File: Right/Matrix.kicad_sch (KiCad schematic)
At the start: 80 parts, among them SW201 SW_Push, SW202 SW_Push, SW203 SW_Push, SW204 SW_Push, SW205 SW_Push, SW206 SW_Push, SW207 SW_Push, SW208 SW_Push, SW209 SW_Push, SW210 SW_Push, SW211 SW_Push, SW212 SW_Push, SW213 SW_Push, SW214 SW_Push, SW215 SW_Push, SW216 SW_Push, SW217 SW_Push, SW218 SW_Push, SW219 SW_Push

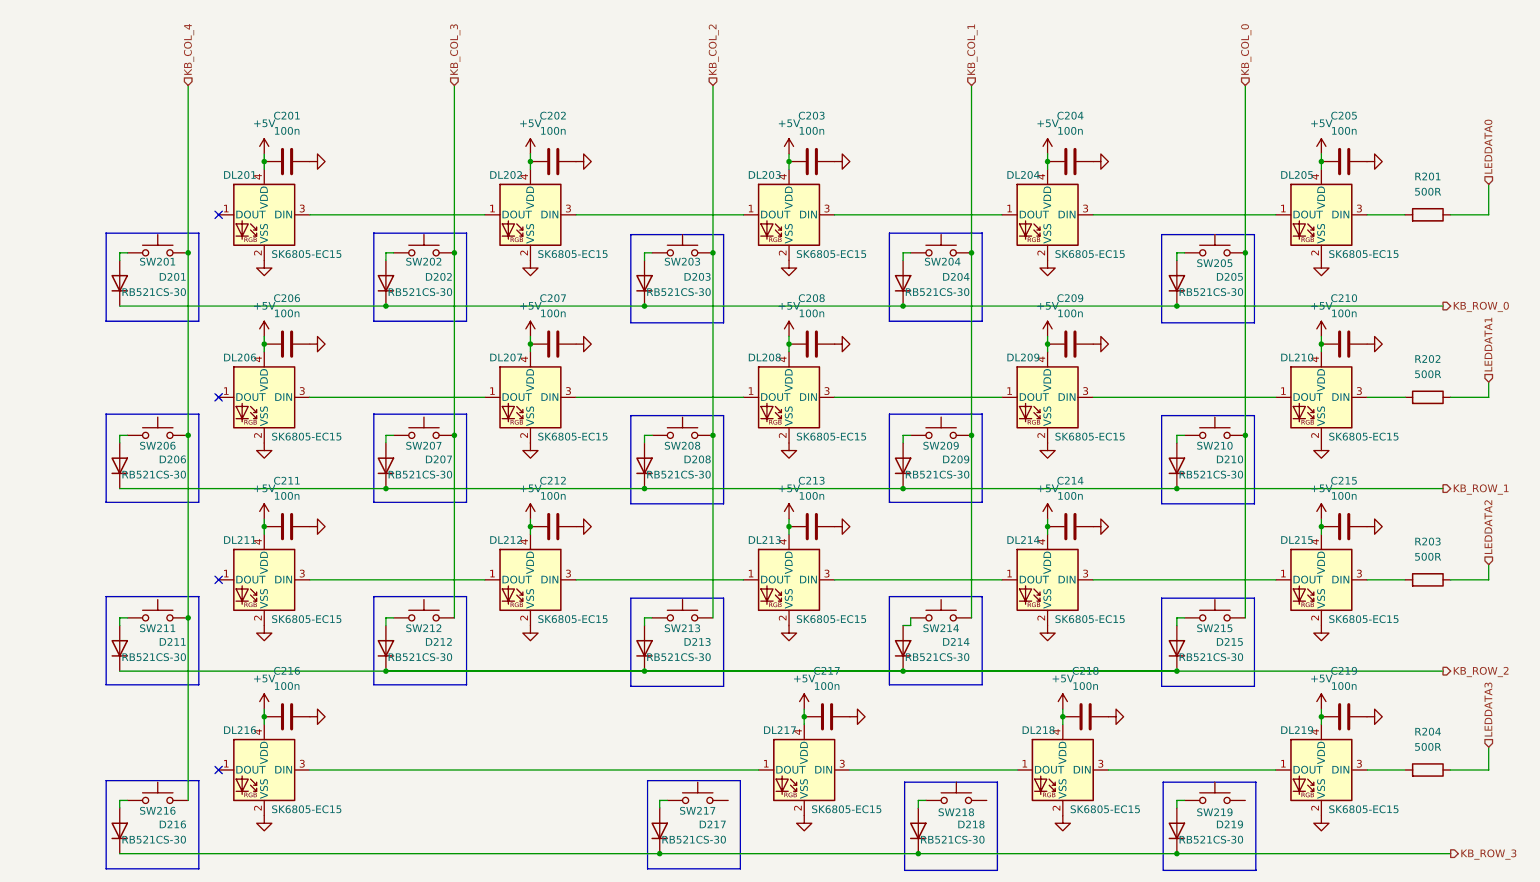
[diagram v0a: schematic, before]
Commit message: redesign with smaller components
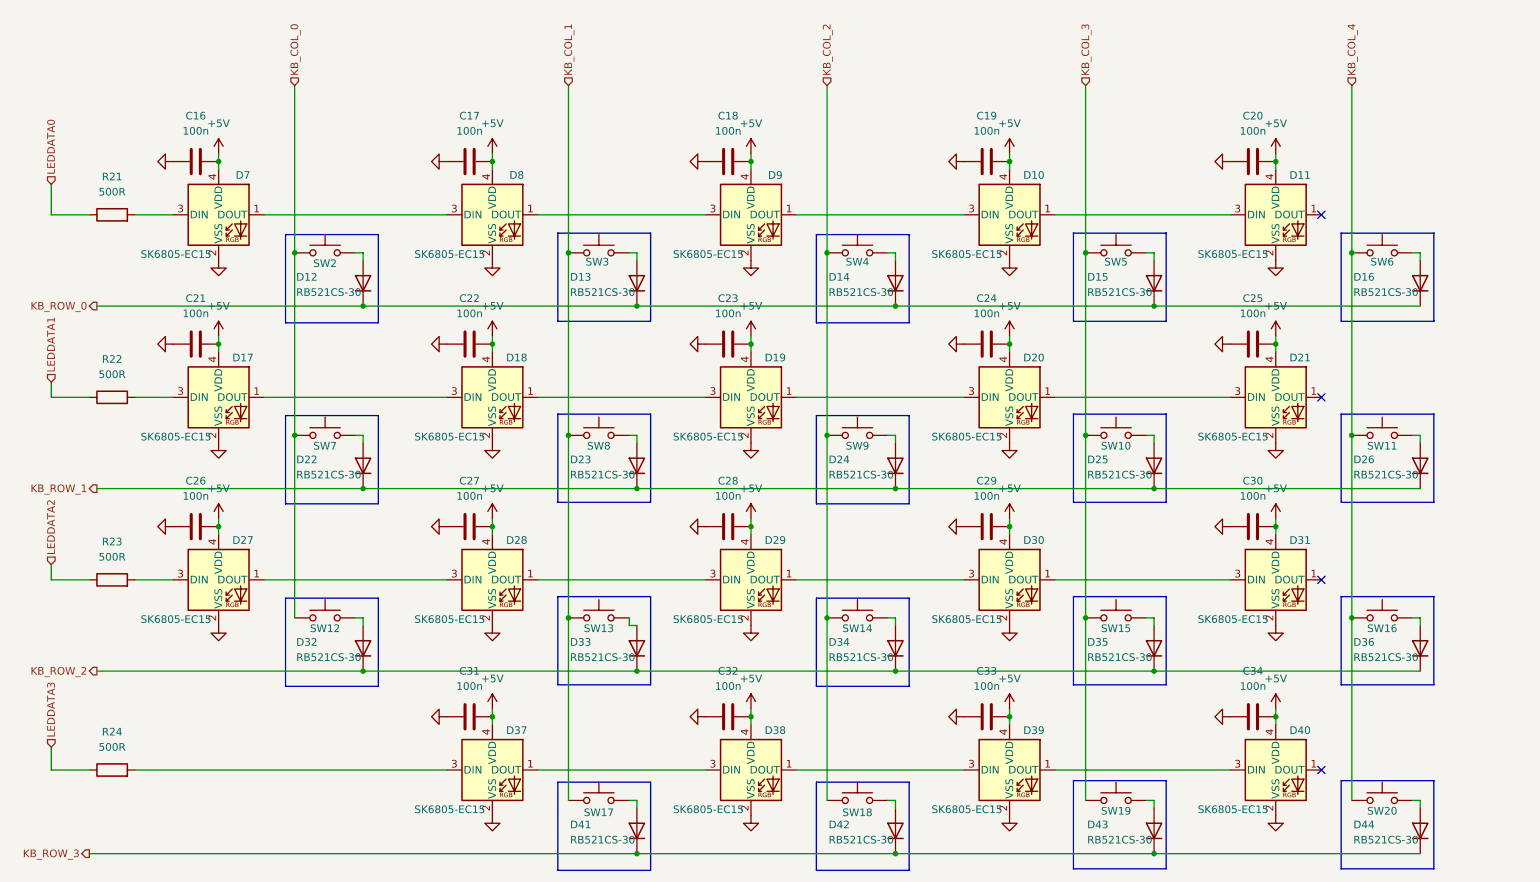
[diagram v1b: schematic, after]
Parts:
- C16: renamed from C205; footprint Capacitor_SMD:C_0603_1608Metric_Pad1.08x0.95mm_HandSolder -> Capacitor_SMD:C_0402_1005Metric_Pad0.74x0.62mm_HandSolder
- C17: renamed from C204; footprint Capacitor_SMD:C_0603_1608Metric_Pad1.08x0.95mm_HandSolder -> Capacitor_SMD:C_0402_1005Metric_Pad0.74x0.62mm_HandSolder
- C18: renamed from C203; footprint Capacitor_SMD:C_0603_1608Metric_Pad1.08x0.95mm_HandSolder -> Capacitor_SMD:C_0402_1005Metric_Pad0.74x0.62mm_HandSolder
- C19: renamed from C202; footprint Capacitor_SMD:C_0603_1608Metric_Pad1.08x0.95mm_HandSolder -> Capacitor_SMD:C_0402_1005Metric_Pad0.74x0.62mm_HandSolder
- C20: renamed from C201; footprint Capacitor_SMD:C_0603_1608Metric_Pad1.08x0.95mm_HandSolder -> Capacitor_SMD:C_0402_1005Metric_Pad0.74x0.62mm_HandSolder
- C21: renamed from C210; footprint Capacitor_SMD:C_0603_1608Metric_Pad1.08x0.95mm_HandSolder -> Capacitor_SMD:C_0402_1005Metric_Pad0.74x0.62mm_HandSolder
- C22: renamed from C209; footprint Capacitor_SMD:C_0603_1608Metric_Pad1.08x0.95mm_HandSolder -> Capacitor_SMD:C_0402_1005Metric_Pad0.74x0.62mm_HandSolder
- C23: renamed from C208; footprint Capacitor_SMD:C_0603_1608Metric_Pad1.08x0.95mm_HandSolder -> Capacitor_SMD:C_0402_1005Metric_Pad0.74x0.62mm_HandSolder
- C24: renamed from C207; footprint Capacitor_SMD:C_0603_1608Metric_Pad1.08x0.95mm_HandSolder -> Capacitor_SMD:C_0402_1005Metric_Pad0.74x0.62mm_HandSolder
- C25: renamed from C206; footprint Capacitor_SMD:C_0603_1608Metric_Pad1.08x0.95mm_HandSolder -> Capacitor_SMD:C_0402_1005Metric_Pad0.74x0.62mm_HandSolder
- C26: renamed from C215; footprint Capacitor_SMD:C_0603_1608Metric_Pad1.08x0.95mm_HandSolder -> Capacitor_SMD:C_0402_1005Metric_Pad0.74x0.62mm_HandSolder
- C27: renamed from C214; footprint Capacitor_SMD:C_0603_1608Metric_Pad1.08x0.95mm_HandSolder -> Capacitor_SMD:C_0402_1005Metric_Pad0.74x0.62mm_HandSolder
- C28: renamed from C213; footprint Capacitor_SMD:C_0603_1608Metric_Pad1.08x0.95mm_HandSolder -> Capacitor_SMD:C_0402_1005Metric_Pad0.74x0.62mm_HandSolder
- C29: renamed from C212; footprint Capacitor_SMD:C_0603_1608Metric_Pad1.08x0.95mm_HandSolder -> Capacitor_SMD:C_0402_1005Metric_Pad0.74x0.62mm_HandSolder
- C30: renamed from C211; footprint Capacitor_SMD:C_0603_1608Metric_Pad1.08x0.95mm_HandSolder -> Capacitor_SMD:C_0402_1005Metric_Pad0.74x0.62mm_HandSolder
- C31: renamed from C219; footprint Capacitor_SMD:C_0603_1608Metric_Pad1.08x0.95mm_HandSolder -> Capacitor_SMD:C_0402_1005Metric_Pad0.74x0.62mm_HandSolder
- C32: renamed from C218; footprint Capacitor_SMD:C_0603_1608Metric_Pad1.08x0.95mm_HandSolder -> Capacitor_SMD:C_0402_1005Metric_Pad0.74x0.62mm_HandSolder
- C33: renamed from C217; footprint Capacitor_SMD:C_0603_1608Metric_Pad1.08x0.95mm_HandSolder -> Capacitor_SMD:C_0402_1005Metric_Pad0.74x0.62mm_HandSolder
- C34: renamed from C216; footprint Capacitor_SMD:C_0603_1608Metric_Pad1.08x0.95mm_HandSolder -> Capacitor_SMD:C_0402_1005Metric_Pad0.74x0.62mm_HandSolder
- R21: renamed from R201; footprint Resistor_SMD:R_0603_1608Metric_Pad0.98x0.95mm_HandSolder -> Resistor_SMD:R_0402_1005Metric_Pad0.72x0.64mm_HandSolder
- R22: renamed from R202; footprint Resistor_SMD:R_0603_1608Metric_Pad0.98x0.95mm_HandSolder -> Resistor_SMD:R_0402_1005Metric_Pad0.72x0.64mm_HandSolder
- R23: renamed from R203; footprint Resistor_SMD:R_0603_1608Metric_Pad0.98x0.95mm_HandSolder -> Resistor_SMD:R_0402_1005Metric_Pad0.72x0.64mm_HandSolder
- R24: renamed from R204; footprint Resistor_SMD:R_0603_1608Metric_Pad0.98x0.95mm_HandSolder -> Resistor_SMD:R_0402_1005Metric_Pad0.72x0.64mm_HandSolder
- renumbered DL202 to D10, DL201 to D11, D205 to D12, D204 to D13, D203 to D14, D202 to D15, D201 to D16, DL210 to D17, DL209 to D18, DL208 to D19, DL207 to D20, DL206 to D21, D210 to D22, D209 to D23, D208 to D24, D207 to D25, D206 to D26, DL215 to D27, DL214 to D28, DL213 to D29, DL212 to D30, DL211 to D31, D215 to D32, D214 to D33, D213 to D34, D212 to D35, D211 to D36, DL219 to D37, DL218 to D38, DL217 to D39, DL216 to D40, D219 to D41, D218 to D42, D217 to D43, D216 to D44, DL205 to D7, DL204 to D8, DL203 to D9, SW207 to SW10, SW206 to SW11, SW215 to SW12, SW214 to SW13, SW213 to SW14, SW212 to SW15, SW211 to SW16, SW219 to SW17, SW218 to SW18, SW217 to SW19, SW205 to SW2, SW216 to SW20, SW204 to SW3, SW203 to SW4, SW202 to SW5, SW201 to SW6, SW210 to SW7, SW209 to SW8, SW208 to SW9
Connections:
- net KB_COL_1: now also SW17.1
- net KB_COL_2: now also SW18.1
- net KB_COL_3: now also SW19.1
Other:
- moved on the sheet: C16, C17, C18, C19, C20, C21, C22, C23, C24, C25, C26, C27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
